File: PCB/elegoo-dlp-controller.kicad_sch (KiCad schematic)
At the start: 6 parts, among them J1 GPIO, U1 CAT24C256

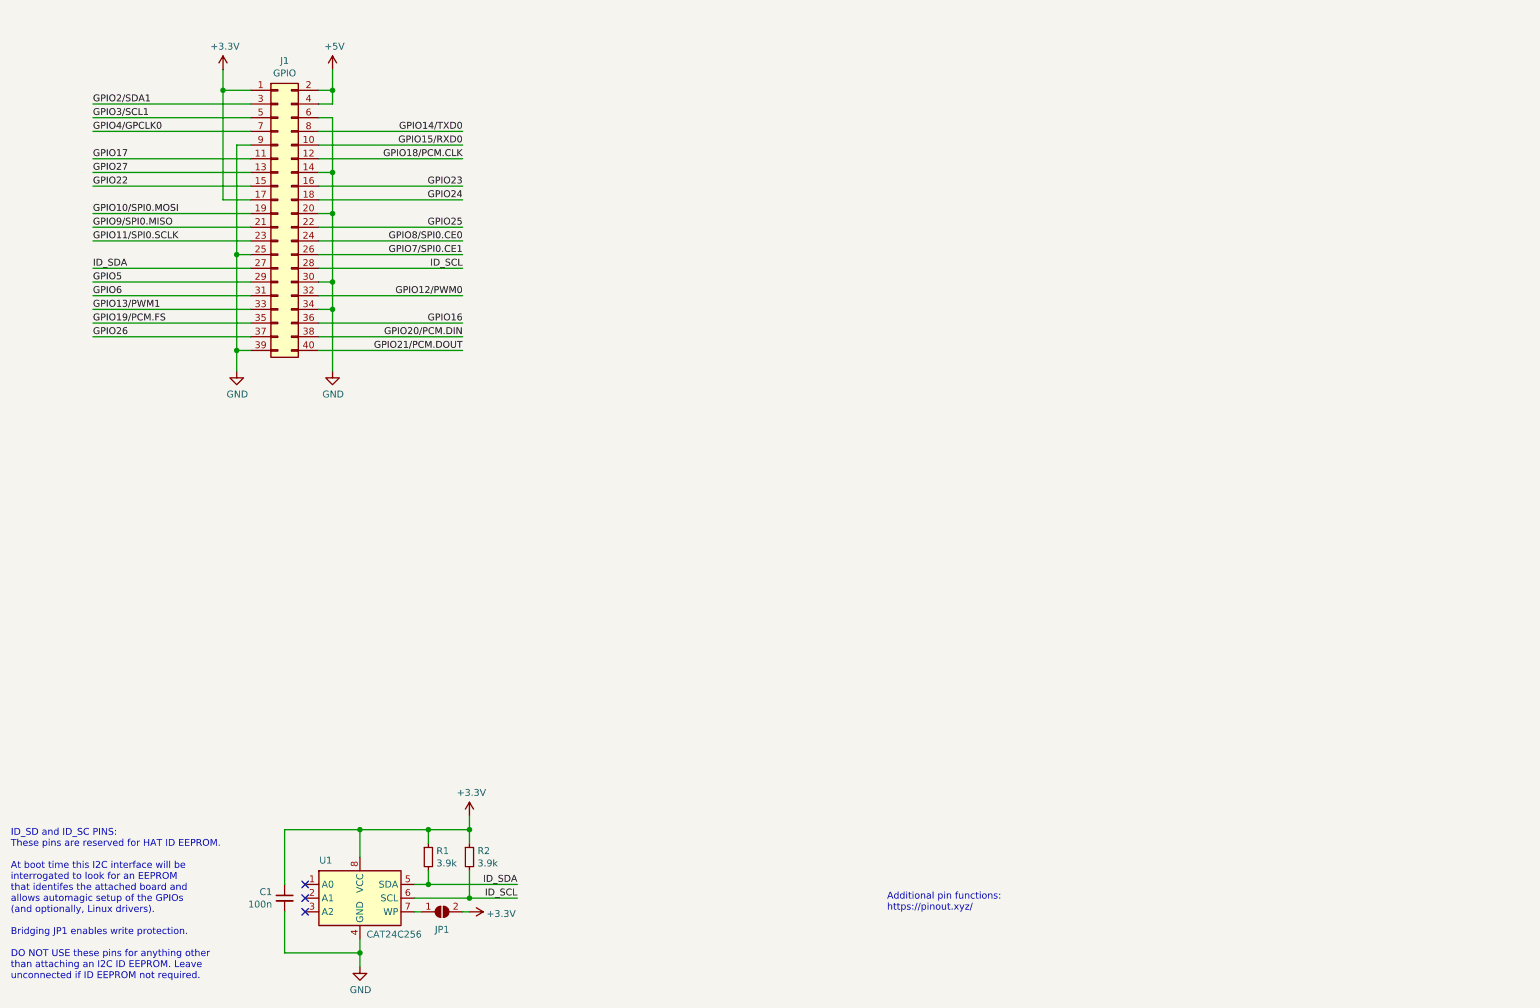
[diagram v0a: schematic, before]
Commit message: Add initial draft of PCB
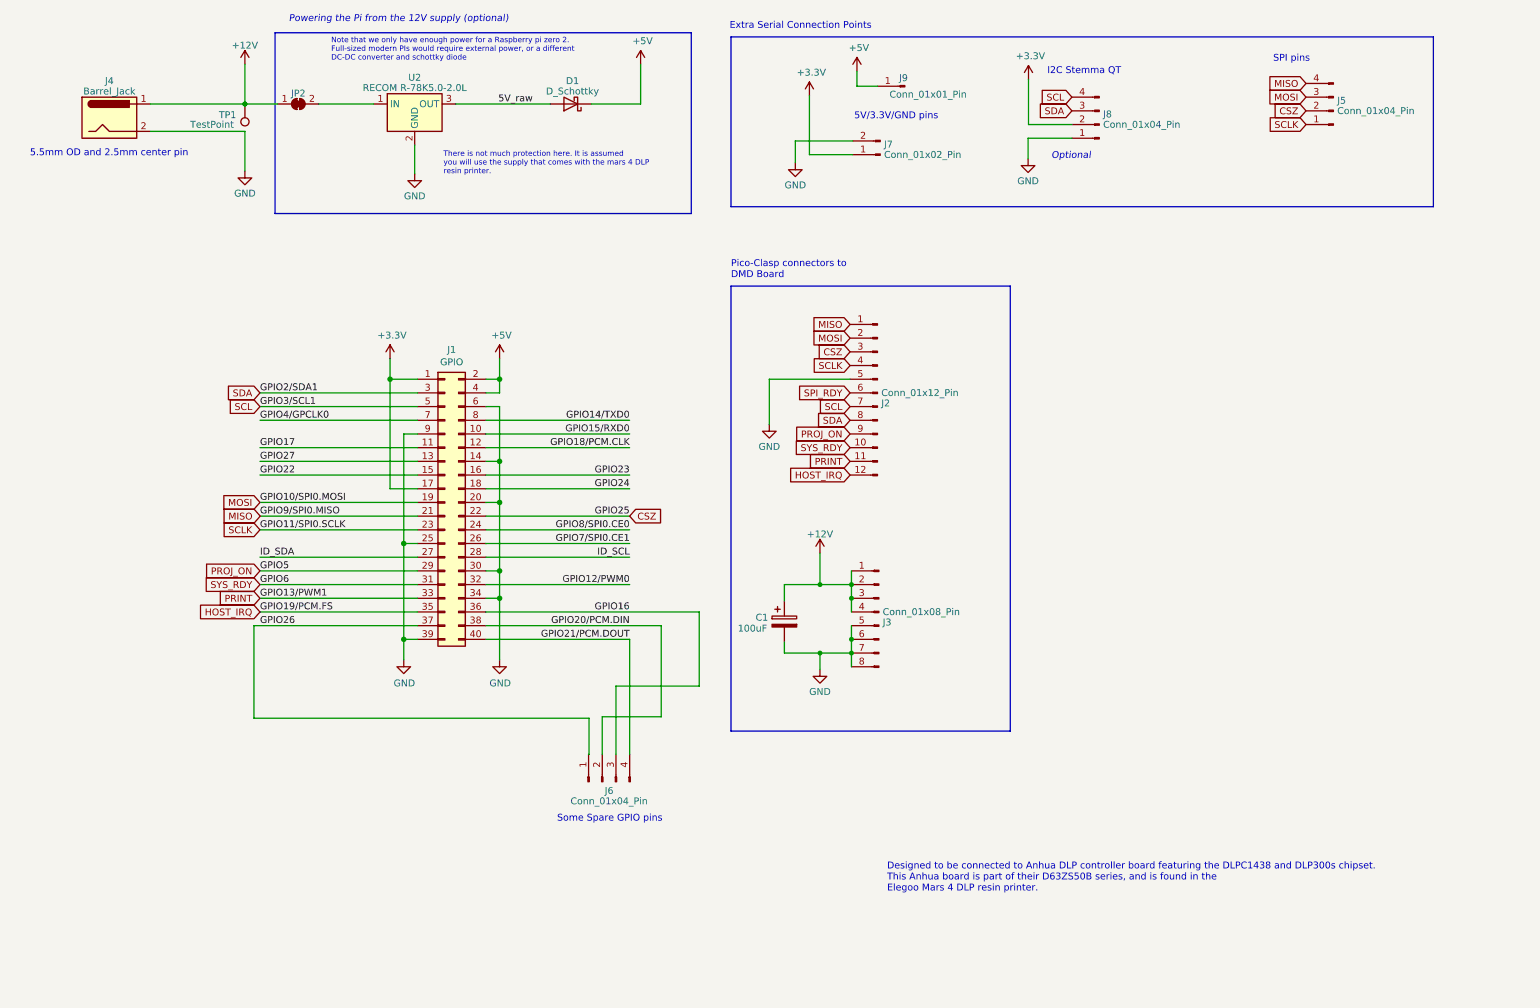
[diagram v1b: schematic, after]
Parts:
- removed C1: 100n, symbol Device:C_Small
- removed JP1: ID_WP, symbol Jumper:SolderJumper_2_Open
- removed R1, R2: 3.9k, symbol Device:R_Small
- removed U1: CAT24C256, symbol Memory_EEPROM:CAT24C256
- added C1: 100uF, Capacitor_SMD:CP_Elec_6.3x5.8, symbol Device:C_Polarized
- added D1: D_Schottky, Diode_SMD:D_SOD-323_HandSoldering, symbol Device:D_Schottky
- added J2: Conn_01x12_Pin, Connector_Molex:Molex_Pico-Clasp_202396-1207_1x12-1MP_P1.00mm_Horizontal, symbol Connector:Conn_01x12_Pin
- added J3: Conn_01x08_Pin, Connector_Molex:Molex_Pico-Clasp_202396-0807_1x08-1MP_P1.00mm_Horizontal, symbol Connector:Conn_01x08_Pin
- added J4: Barrel_Jack, Connector_BarrelJack:BarrelJack_GCT_DCJ200-10-A_Horizontal, symbol Connector:Barrel_Jack
- added J5: Conn_01x04_Pin, Connector_PinHeader_2.54mm:PinHeader_1x04_P2.54mm_Vertical, symbol Connector:Conn_01x04_Pin
- added J6: Conn_01x04_Pin, Connector_PinHeader_2.54mm:PinHeader_2x02_P2.54mm_Vertical, symbol Connector:Conn_01x04_Pin
- added J7: Conn_01x02_Pin, Connector_PinHeader_2.54mm:PinHeader_1x02_P2.54mm_Vertical, symbol Connector:Conn_01x02_Pin
- added J8: Conn_01x04_Pin, Connector_JST:JST_SH_SM04B-SRSS-TB_1x04-1MP_P1.00mm_Horizontal, symbol Connector:Conn_01x04_Pin
- added J9: Conn_01x01_Pin, Connector_PinHeader_2.54mm:PinHeader_1x01_P2.54mm_Vertical, symbol Connector:Conn_01x01_Pin
- added JP2: SolderJumper_2_Bridged, Jumper:SolderJumper-2_P1.3mm_Open_TrianglePad1.0x1.5mm, symbol Jumper:SolderJumper_2_Bridged
- added TP1: TestPoint, TestPoint:TestPoint_Pad_D1.5mm, symbol Connector:TestPoint
- added U2: RECOM R-78K5.0-2.0L, Converter_DCDC:Converter_DCDC_RECOM_R-78HB-0.5L_THT, symbol Converter_DCDC:OKI-78SR-3.3_1.5-W36-C
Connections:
- net +3V3: now also J7.1 (Pin_1), J8.2 (Pin_2)
- net +5V: now also D1.1 (K), J9.1 (Pin_1)
- net GND: now also C1.2, J2.5 (Pin_5), J3.5 (Pin_5), J3.6 (Pin_6), J3.7 (Pin_7), J3.8 (Pin_8), J4.2, J7.2 (Pin_2), J8.1 (Pin_1), U2.2 (GND)
- net GPIO16: now also J6.3 (Pin_3)
- net GPIO20/PCM.DIN: now also J6.2 (Pin_2)
- net GPIO21/PCM.DOUT: now also J6.4 (Pin_4)
- net GPIO26: now also J6.1 (Pin_1)
- net GPIO10/SPI0.MOSI renamed MOSI
- net MOSI: now also J2.2 (Pin_2), J5.3 (Pin_3)
- net GPIO11/SPI0.SCLK renamed SCLK
- net SCLK: now also J2.4 (Pin_4), J5.1 (Pin_1)
- net GPIO13/PWM1 renamed PRINT
- net PRINT: now also J2.11 (Pin_11)
- net GPIO19/PCM.FS renamed HOST_IRQ
- net HOST_IRQ: now also J2.12 (Pin_12)
- net GPIO25 renamed CSZ
- net CSZ: now also J2.3 (Pin_3), J5.2 (Pin_2)
- net GPIO2/SDA1 renamed SDA
- net SDA: now also J2.8 (Pin_8), J8.3 (Pin_3)
- net GPIO3/SCL1 renamed SCL
- net SCL: now also J2.7 (Pin_7), J8.4 (Pin_4)
- net GPIO5 renamed PROJ_ON
- net PROJ_ON: now also J2.9 (Pin_9)
- net GPIO6 renamed SYS_RDY
- net SYS_RDY: now also J2.10 (Pin_10)
- net GPIO9/SPI0.MISO renamed MISO
- net MISO: now also J2.1 (Pin_1), J5.4 (Pin_4)
- new net: JP2.2 (B), U2.1 (IN)
- new net +12V: C1.1, J3.1 (Pin_1), J3.2 (Pin_2), J3.3 (Pin_3), J3.4 (Pin_4), J4.1, JP2.1 (A), TP1.1
- new net 5V_raw: D1.2 (A), U2.3 (OUT)
- new net SPI_RDY: J2.6 (Pin_6)
- no-connect marks 3 -> 0
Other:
- note added: "5.5mm OD and 2.5mm center pin"
- note added: "5V/3.3V/GND pins"
- note added: "Designed to be connected to Anhua DLP controller board featuring the DLPC1438 and DLP300s chipset. This Anhua board is part of their D63ZS50B series, and is found in the Elegoo Mars 4 DLP resin printer."
- note added: "Extra Serial Connection Points"
- note added: "I2C Stemma QT"
- note added: "Note that we only have enough power for a Raspberry pi zero 2. Full-sized modern PIs would require external power, or a different DC-DC converter and schottky diode"
- note added: "Optional"
- note added: "Pico-Clasp connectors to DMD Board"
- note added: "Powering the Pi from the 12V supply (optional)"
- note added: "SPI pins"
- note added: "Some Spare GPIO pins"
- note added: "There is not much protection here. It is assumed you will use the supply that comes with the mars 4 DLP resin printer."
- note removed: "Additional pin functions: https://pinout.xyz/"
- note removed: "ID_SD and ID_SC PINS: These pins are reserved for HAT ID EEPROM. At boot time this I2C interface will be interrogated to look for an EEPROM that identifes the attached board and allows automagic setup of the GPIOs (and optionally, Linux drivers). Bridging JP1 enables write protection. DO NOT USE these pins for anything other than attaching an I2C ID EEPROM. Leave unconnected if ID EEPROM not requ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"
- title: (none) -> Raspberry pi DMD controller board
- moved on the sheet: J1

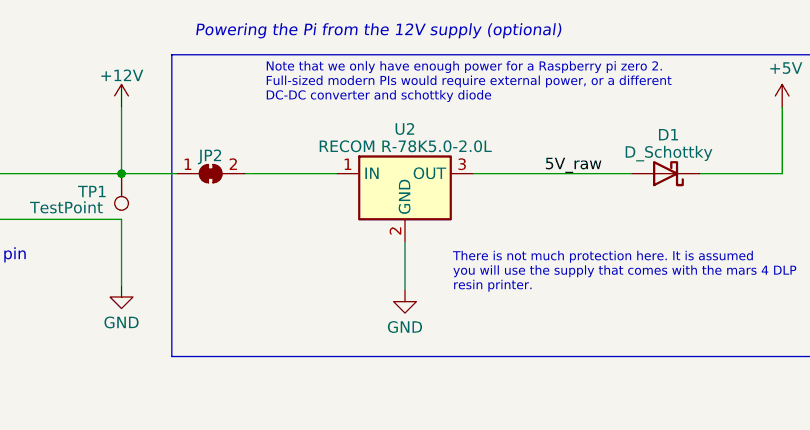
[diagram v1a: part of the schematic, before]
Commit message: change dc converter and switch to vertical connectors
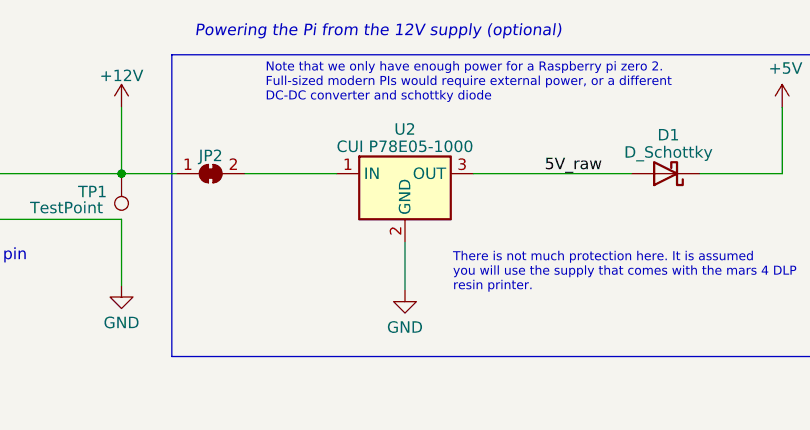
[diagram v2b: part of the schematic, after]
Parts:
- J2: footprint Connector_Molex:Molex_Pico-Clasp_202396-1207_1x12-1MP_P1.00mm_Horizontal -> Connector_Molex:Molex_Pico-Clasp_501331-1207_1x12-1MP_P1.00mm_Vertical; Mouser 538-202396-1207 -> 538-501331-1207
- J3: footprint Connector_Molex:Molex_Pico-Clasp_202396-0807_1x08-1MP_P1.00mm_Horizontal -> Connector_Molex:Molex_Pico-Clasp_501331-0807_1x08-1MP_P1.00mm_Vertical; Mouser 538-501568-0807 -> 538-501331-0807
- U2: value RECOM R-78K5.0-2.0L -> CUI P78E05-1000; footprint Converter_DCDC:Converter_DCDC_RECOM_R-78HB-0.5L_THT -> Converter_DCDC:Converter_DCDC_RECOM_R-78E-0.5_THT; Mouser 919-R-78K5.0-2.0L -> 490-P78E05-1000
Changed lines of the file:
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@@
       (effects (font (size 1.27 1.27)) (justify right))
     )
-    (property "Footprint" "Connector_Molex:Molex_Pico-Clasp_202396-0807_1x08-1MP_P1.00mm_Horizontal" (at 177.546 124.714 0)
+    (property "Footprint" "Connector_Molex:Molex_Pico-Clasp_501331-0807_1x08-1MP_P1.00mm_Vertical" (at 177.546 124.714 0)
       (effects (font (size 1.27 1.27)) hide)
     )
@@
       (effects (font (size 1.27 1.27)) hide)
     )
-    (property "Mouser" "538-501568-0807" (at 177.546 124.714 0)
+    (property "Mouser" "538-501331-0807" (at 177.546 124.714 0)
       (effects (font (size 1.27 1.27)) hide)
     )
@@
       (effects (font (size 1.27 1.27)))
     )
-    (property "Value" "RECOM R-78K5.0-2.0L" (at 91.44 27.4861 0)
+    (property "Value" "CUI P78E05-1000" (at 91.44 27.4861 0)
       (effects (font (size 1.27 1.27)))
     )
-    (property "Footprint" "Converter_DCDC:Converter_DCDC_RECOM_R-78HB-0.5L_THT" (at 92.71 36.83 0)
+    (property "Footprint" "Converter_DCDC:Converter_DCDC_RECOM_R-78E-0.5_THT" (at 92.71 36.83 0)
       (effects (font (size 1.27 1.27) italic) (justify left) hide)
     )
@@
       (effects (font (size 1.27 1.27)) hide)
     )
-    (property "Mouser" "919-R-78K5.0-2.0L" (at 91.44 30.48 0)
+    (property "Mouser" "490-P78E05-1000" (at 91.44 30.48 0)
       (effects (font (size 1.27 1.27)) hide)
     )
@@
       (effects (font (size 1.27 1.27)) (justify right))
     )
-    (property "Footprint" "Connector_Molex:Molex_Pico-Clasp_202396-1207_1x12-1MP_P1.00mm_Horizontal" (at 177.292 84.074 0)
+    (property "Footprint" "Connector_Molex:Molex_Pico-Clasp_501331-1207_1x12-1MP_P1.00mm_Vertical" (at 177.292 84.074 0)
       (effects (font (size 1.27 1.27)) hide)
     )
@@
       (effects (font (size 1.27 1.27)) hide)
     )
-    (property "Mouser" "538-202396-1207" (at 177.292 84.074 0)
+    (property "Mouser" "538-501331-1207" (at 177.292 84.074 0)
       (effects (font (size 1.27 1.27)) hide)
     )

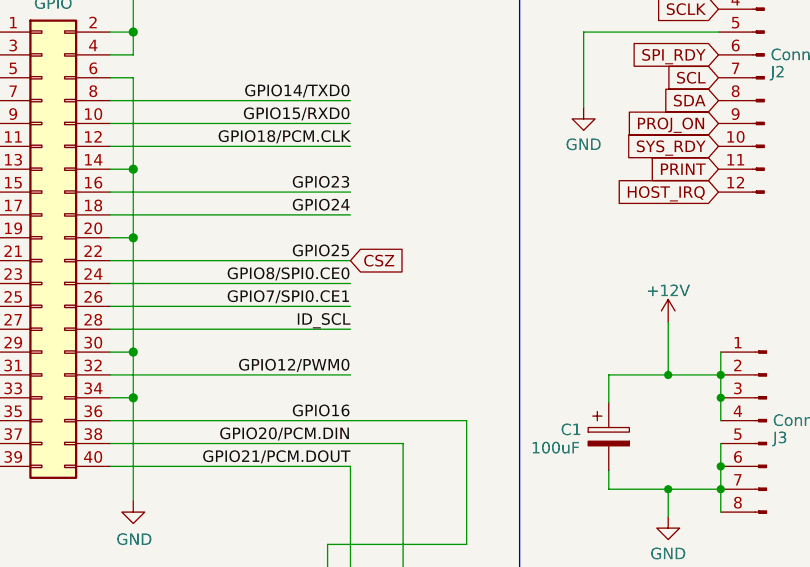
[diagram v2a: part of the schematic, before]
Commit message: Connect SPI_RDY and minor retouching
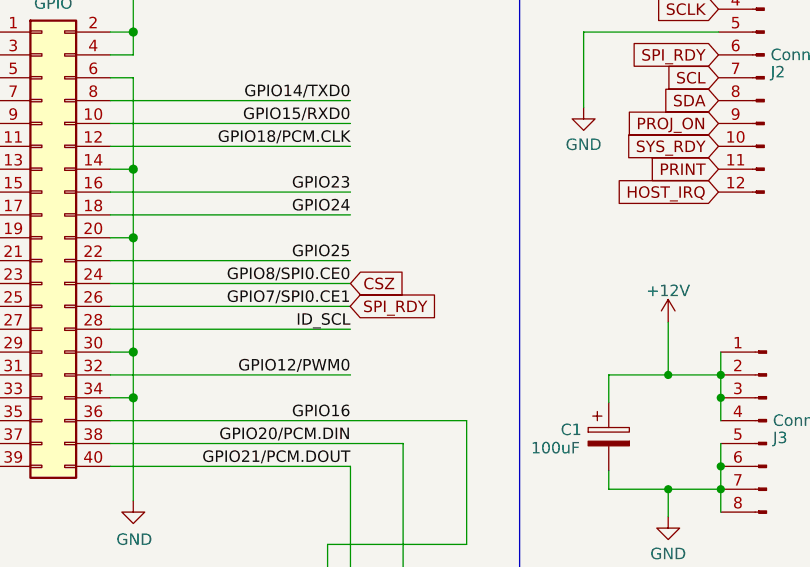
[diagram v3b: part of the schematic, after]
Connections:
- net GPIO7/SPI0.CE1 is gone; now on net SPI_RDY: J1.26 (Pin_26)
- net GPIO8/SPI0.CE0 is gone; now on net CSZ: J1.24 (Pin_24)
- net CSZ: no longer J1.22 (Pin_22)
- new net GPIO25: J1.22 (Pin_22)
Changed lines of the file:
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@@
     (effects (font (size 1.27 1.27)) (justify left bottom))
+  )
+  (global_label "CSZ" (shape input) (at 131.318 109.474 0) (fields_autoplaced)
+    (effects (font (size 1.27 1.27)) (justify left))
+    (property "Intersheetrefs" "${INTERSHEET_REFS}" (at 138.0079 109.474 0)
+      (effects (font (size 1.27 1.27)) (justify left) hide)
+    )
   )
   (global_label "SYS_RDY" (shape input) (at 172.212 94.234 180) (fields_autoplaced)
@@
     )
   )
+  (global_label "SPI_RDY" (shape input) (at 131.2831 112.014 0) (fields_autoplaced)
+    (effects (font (size 1.27 1.27)) (justify left))
+    (property "Intersheetrefs" "${INTERSHEET_REFS}" (at 141.9645 112.014 0)
+      (effects (font (size 1.27 1.27)) (justify left) hide)
+    )
+  )
   (global_label "SYS_RDY" (shape input) (at 62.738 119.634 180) (fields_autoplaced)
     (effects (font (size 1.27 1.27)) (justify right))
@@
     )
   )
-  (global_label "CSZ" (shape input) (at 131.318 106.934 0) (fields_autoplaced)
-    (effects (font (size 1.27 1.27)) (justify left))
-    (property "Intersheetrefs" "${INTERSHEET_REFS}" (at 138.0079 106.934 0)
-      (effects (font (size 1.27 1.27)) (justify left) hide)
-    )
-  )

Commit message: Add PCB readme and BOM
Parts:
- J8: Mouser 485-4208 -> 474-PRT-14417
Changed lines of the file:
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@@
       (effects (font (size 1.27 1.27)) hide)
     )
-    (property "Datasheet" "~" (at 218.44 34.29 0)
+    (property "Datasheet" "https://nl.mouser.com/datasheet/2/813/Qwiic_Connector_Datasheet-1223982.pdf" (at 218.44 34.29 0)
       (effects (font (size 1.27 1.27)) hide)
     )
-    (property "Mouser" "485-4208" (at 218.44 34.29 0)
+    (property "Mouser" "474-PRT-14417" (at 218.44 34.29 0)
       (effects (font (size 1.27 1.27)) hide)
     )
